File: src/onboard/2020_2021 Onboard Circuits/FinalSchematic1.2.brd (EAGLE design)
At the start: 137.6 x 80 mm, 99 parts, among them IC1 A5975D, IC2 A5975D, IC3 A5975D

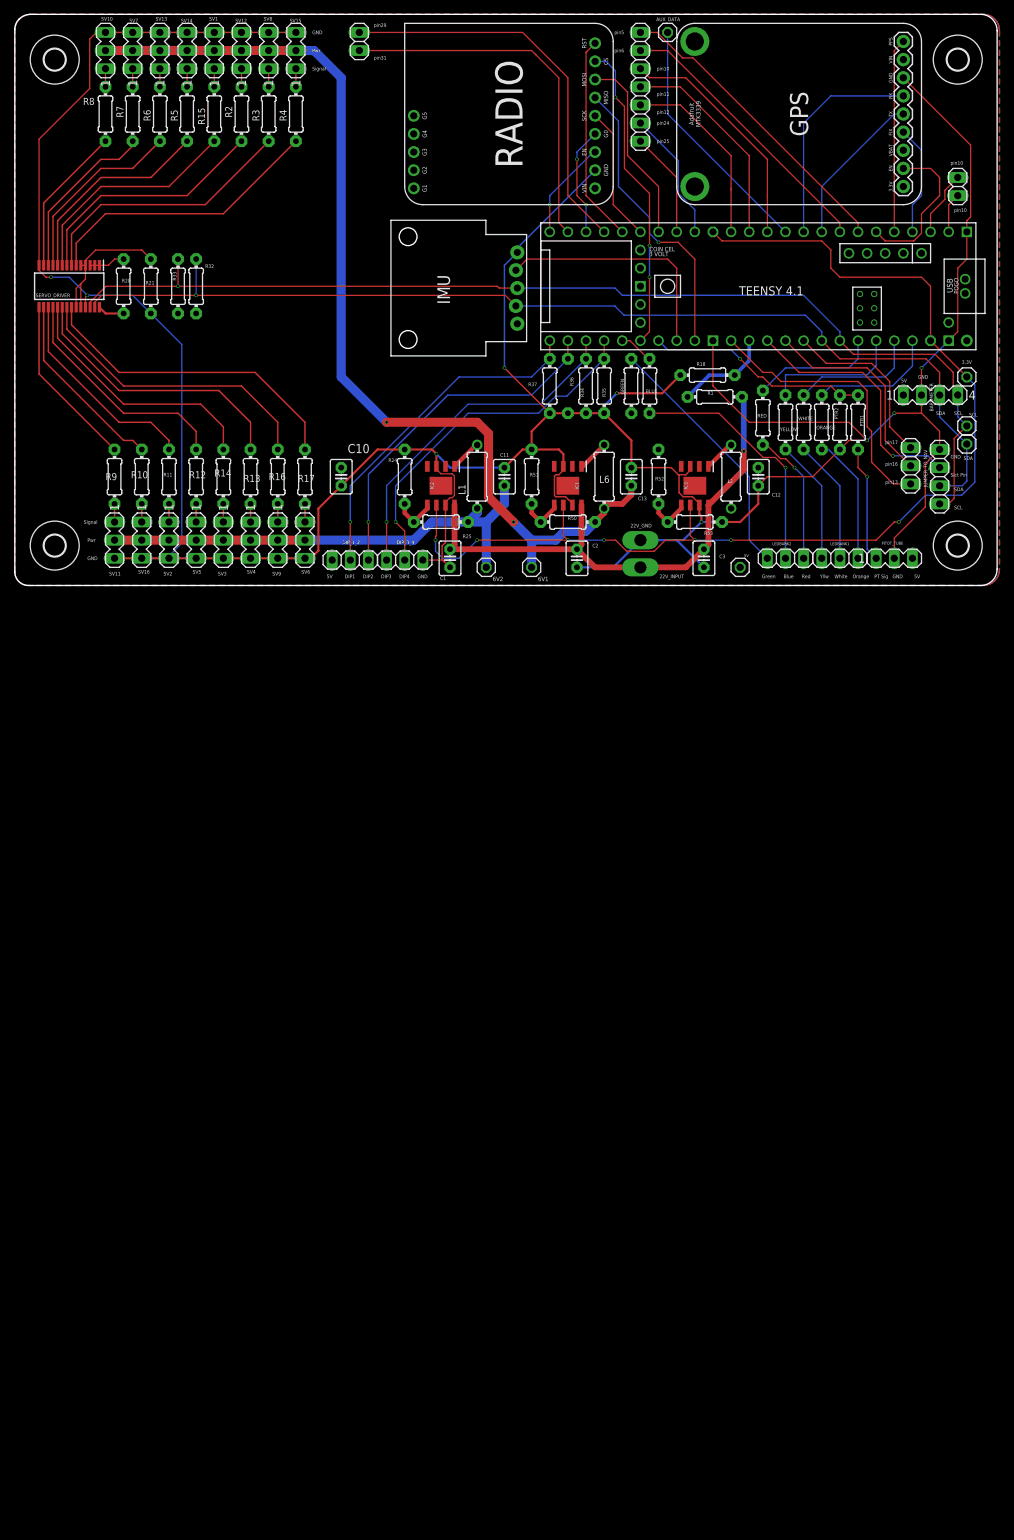
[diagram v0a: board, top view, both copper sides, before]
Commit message: Added button connection, rewired radio, removed pitot tube, split into pages
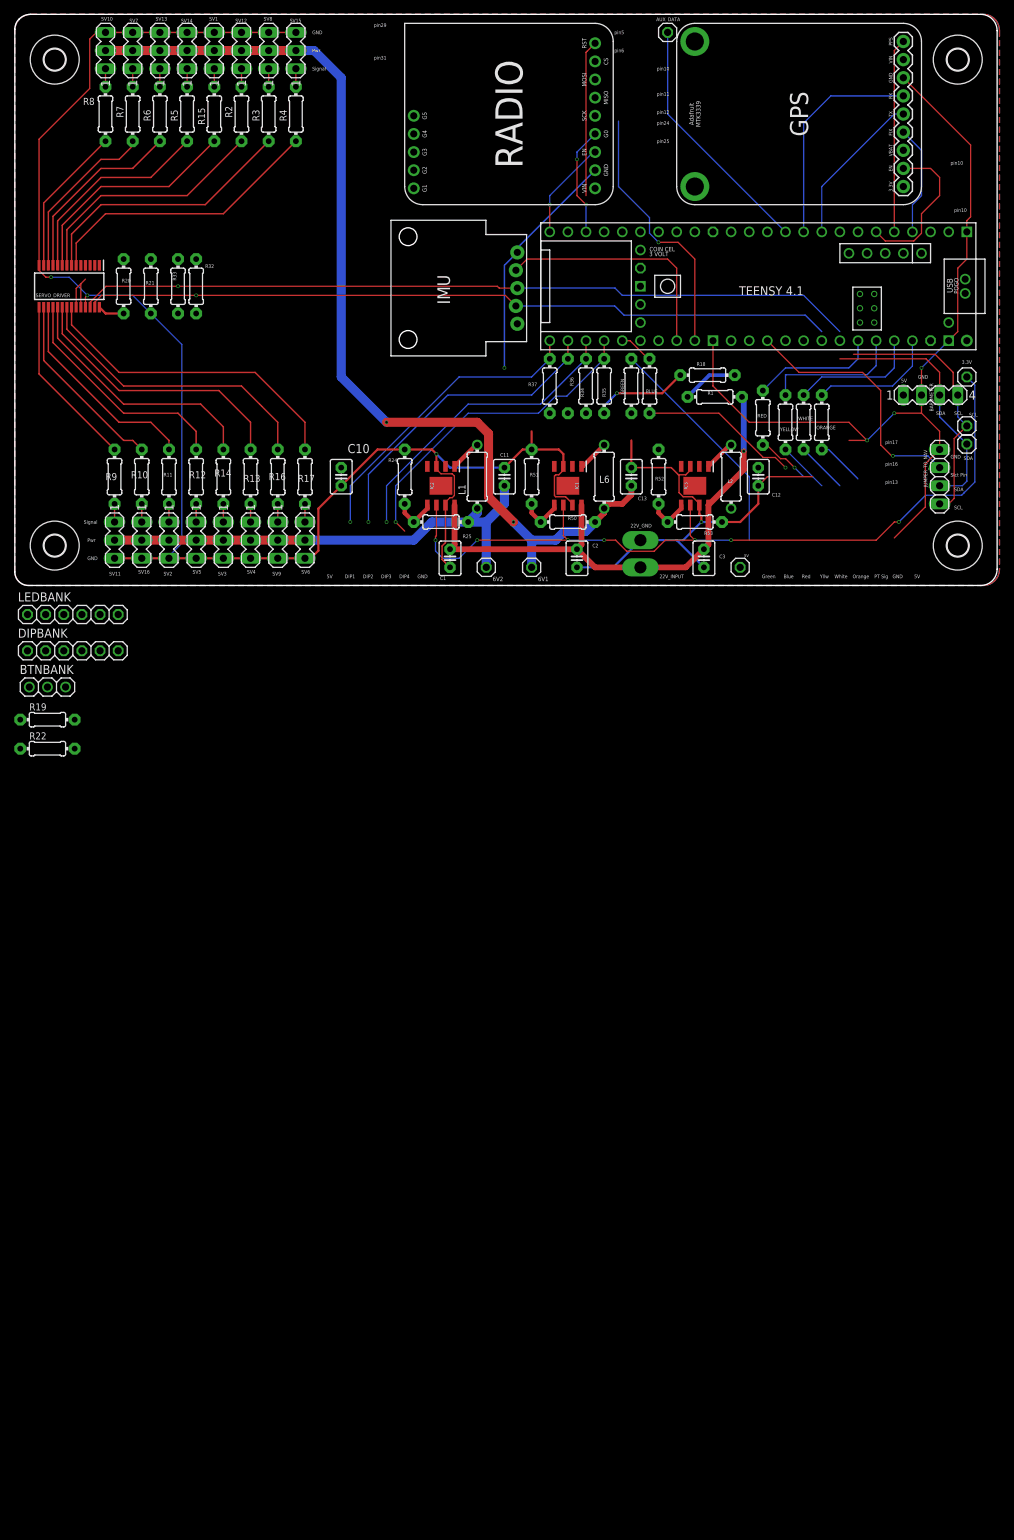
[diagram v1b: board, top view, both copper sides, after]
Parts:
- removed 1, 2, 5: (no value), pinhead:1X02
- removed 4: (no value), pinhead:1X05
- removed DIP_1_2, DIP_3_4, JP1, LEDBANK1, LEDBANK2: (no value), pinhead:1X03
- removed PITOT_TUBE: (no value), con-lstb:MA03-1
- removed PTR1: 2.2K, adafruit:0204/7
- removed PTR2: 4.3K, adafruit:0204/7
- added BTNBANK: (no value), adafruit:1X03
- added DIPBANK, LEDBANK: (no value), adafruit:1X06
- added R19, R22: 2.2k, adafruit:0204/7
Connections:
- removed net MOSI1: RADIO.7, TEENSY4.1.26-A12/MOSI1
- removed net N$4: PITOT_TUBE.1, PTR1.2
- removed net PIN0: 2.2, TEENSY4.1.0-RX1/CS1/CRX2
- removed net PIN1: 2.1, TEENSY4.1.1-TX1/MISO1/CTX2
- removed net PIN10: 4.5, TEENSY4.1.10-CS\MQSR
- removed net PIN11: 4.4, TEENSY4.1.11-MOSI/CTX1
- removed net PIN12: 4.3, TEENSY4.1.12-MISO/MQSL
- removed net PIN13: JP1.3, TEENSY4.1.13-SCK/LED
- removed net PIN14: R1.1, R18.2, TEENSY4.1.14-A0/TX3/SPDIF_OUT
- removed net PIN16: JP1.2, TEENSY4.1.16-A2/RX4/SCL1
- removed net PIN17: JP1.1, TEENSY4.1.17-A3/TX4/SDA1
- removed net PIN24: 4.2, TEENSY4.1.24-A10/TX6/SCL2
- removed net PIN25: 4.1, TEENSY4.1.25-A11/RX6/SDA2
- removed net PIN29: 1.2, TEENSY4.1.29-TX7
- removed net PIN31: 1.1, TEENSY4.1.31-CTX3
- removed net PIN5: 5.2, TEENSY4.1.5-IN2
- removed net PIN6: 5.1, TEENSY4.1.6-OUT1D
- removed net PT_ANLGPIN: PTR1.1, PTR2.2, TEENSY4.1.39-A15/CS/OUT1A
- removed net RADIO_CS: RADIO.8, TEENSY4.1.38-A14/CS/IN1
- removed net SCK1: RADIO.5, TEENSY4.1.27-A13/SCK1
- new net BATLEVEL: R1.1, R18.2
- new net CS0: RADIO.8, TEENSY4.1.10-CS\MQSR
- new net MISO0: RADIO.6, TEENSY4.1.12-MISO/MQSL
- new net MOSI0: RADIO.7, TEENSY4.1.11-MOSI/CTX1
- new net N$3: BTNBANK.1, R22.2
- new net N$5: BTNBANK.2, R19.2
- new net SCK0: RADIO.5, TEENSY4.1.13-SCK/LED
- net 3.3V: now also TEENSY4.1.3V3-2
- net 5V: now also BTNBANK.3, DIPBANK.6, R33.2; no longer DIP_1_2.3, PITOT_TUBE.3, R33.1
- net BLUE: now also LEDBANK.5; no longer LEDBANK2.2
- net DIP1: now also DIPBANK.5; no longer DIP_1_2.2
- net DIP2: now also DIPBANK.4; no longer DIP_1_2.1
- net DIP3: now also DIPBANK.3; no longer DIP_3_4.3
- net DIP4: now also DIPBANK.2; no longer DIP_3_4.2
- net GND: now also DIPBANK.1, R19.1, R22.1, TEENSY4.1.GND2, TEENSY4.1.GND4, TEENSY4.1.GND5; no longer DIP_3_4.1, PITOT_TUBE.2, PTR2.1
- net GNDADDRESS: no longer R21.2
- net GREEN: now also LEDBANK.6; no longer LEDBANK2.3
- net MISO1: no longer RADIO.6
- net ORANGE: now also LEDBANK.1; no longer LEDBANK1.1
- net RADIO_RST: now also TEENSY4.1.6-OUT1D; no longer TEENSY4.1.28-RX7
- net RED: now also LEDBANK.4; no longer LEDBANK2.1
- net SCL: now also R32.1; no longer R33.2
- net SDA: now also R33.1; no longer R32.1
- net WHITE: now also LEDBANK.2; no longer LEDBANK1.2
- net YELLOW: now also LEDBANK.3; no longer LEDBANK1.3
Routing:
- net PIN29: track 55.5 -> 0.00 mm
- net PIN31: track 51.6 -> 0.00 mm
- net 3.3V: track 163.6 -> 113.7 mm
- net RADIO_CS: track 43.7 -> 0.00 mm, vias 3 -> 0
- net PIN5: track 42.8 -> 0.00 mm
- net GND: track 499.0 -> 459.6 mm
- net PIN6: track 39.2 -> 0.00 mm
- net PIN13: track 39.0 -> 0.00 mm
- net PIN10: track 33.2 -> 0.00 mm
- net PT_ANLGPIN: track 31.1 -> 0.00 mm, vias 1 -> 0
- net PIN11: track 29.9 -> 0.00 mm
- net PIN16: track 29.2 -> 0.00 mm
- net MOSI1: track 26.7 -> 0.00 mm
- net PIN12: track 26.3 -> 0.00 mm
- net PIN17: track 24.9 -> 0.00 mm
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
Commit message: Added 5v connector
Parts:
- removed DIPBANK: (no value), adafruit:1X06
- added 5V_PWR: (no value), pinhead:1X03
- added DIPBANK1: (no value), pinhead:1X05
- BTNBANK: device adafruit:1X03 -> pinhead:1X03
- LEDBANK: device adafruit:1X06 -> pinhead:1X06
- moved LEDBANK 29.5 mm to (-27.4, -33.5)
- moved BTNBANK 24.9 mm to (-31.0, -39.1)
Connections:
- net 5V: now also 5V_PWR.1, 5V_PWR.2, DIPBANK1.5; no longer DIPBANK.6
- net DIP1: now also DIPBANK1.4; no longer DIPBANK.5
- net DIP2: now also DIPBANK1.3; no longer DIPBANK.4
- net DIP3: now also DIPBANK1.2; no longer DIPBANK.3
- net DIP4: now also DIPBANK1.1; no longer DIPBANK.2
- net GND: now also 5V_PWR.3; no longer DIPBANK.1

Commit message: Added button wires and fixed 5v input
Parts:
- LEDBANK: device pinhead:1X06 -> pinhead:1X07
- moved LEDBANK 22.4 mm to (-25.9, -55.9)
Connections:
- removed net N$3: BTNBANK.1, R22.2
- removed net N$5: BTNBANK.2, R19.2
- new net BTN1: BTNBANK.2, R19.2, TEENSY4.1.24-A10/TX6/SCL2
- new net BTN2: BTNBANK.1, R22.2, TEENSY4.1.25-A11/RX6/SDA2
- net 5V: now also SV1.2, SV10.2, SV11.2, SV12.2, SV13.2, SV14.2, SV15.2, SV16.2, SV2.2, SV3.2, SV4.2, SV5.2, SV6.2, SV7.2, SV8.2, SV9.2
- net BATLEVEL: now also TEENSY4.1.26-A12/MOSI1
- net BLUE: now also LEDBANK.6; no longer LEDBANK.5
- net GND: now also LEDBANK.1
- net GNDADDRESS: now also R21.2
- net GREEN: now also LEDBANK.7; no longer LEDBANK.6
- net ORANGE: now also LEDBANK.2; no longer LEDBANK.1
- net OUTPUT_BUCK1: no longer SV1.2, SV10.2, SV12.2, SV13.2, SV14.2, SV15.2, SV7.2, SV8.2
- net OUTPUT_BUCK2: no longer SV11.2, SV16.2, SV2.2, SV3.2, SV4.2, SV5.2, SV6.2, SV9.2
- net RED: now also LEDBANK.5; no longer LEDBANK.4
- net WHITE: now also LEDBANK.3; no longer LEDBANK.2
- net YELLOW: now also LEDBANK.4; no longer LEDBANK.3
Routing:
- net 5V: track 3.76 -> 83.8 mm
- net OUTPUT_BUCK2: track 94.7 -> 26.1 mm
- net OUTPUT_BUCK1: track 139.9 -> 110.7 mm

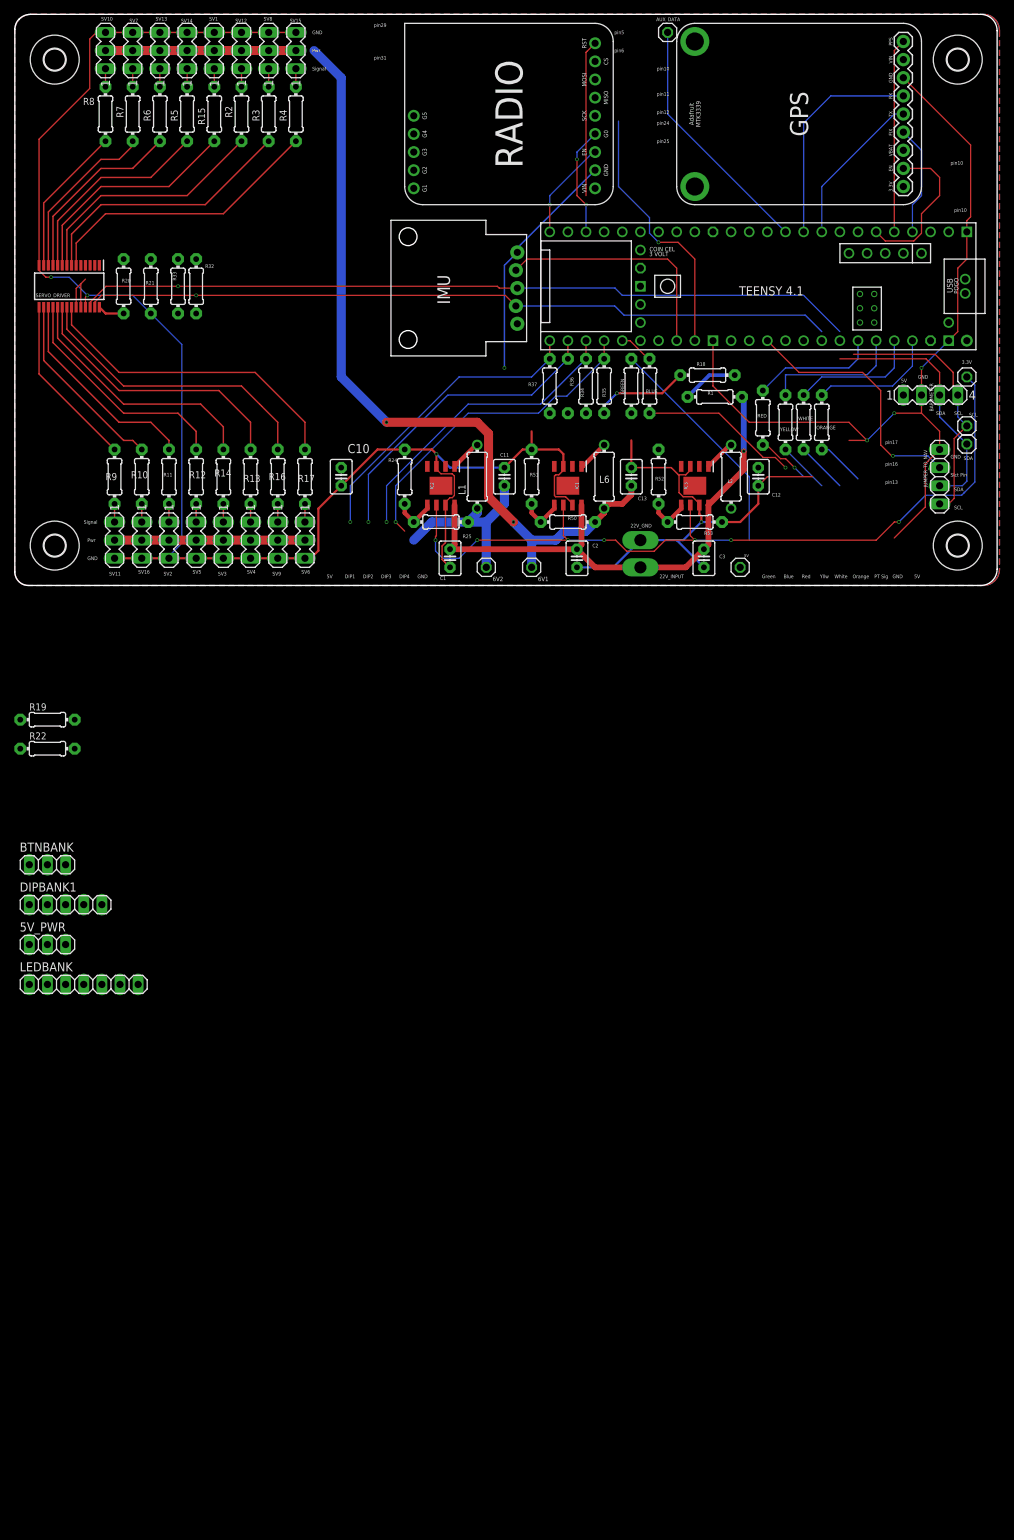
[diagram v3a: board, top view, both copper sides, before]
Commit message: Added 6v->5v LDO regulator
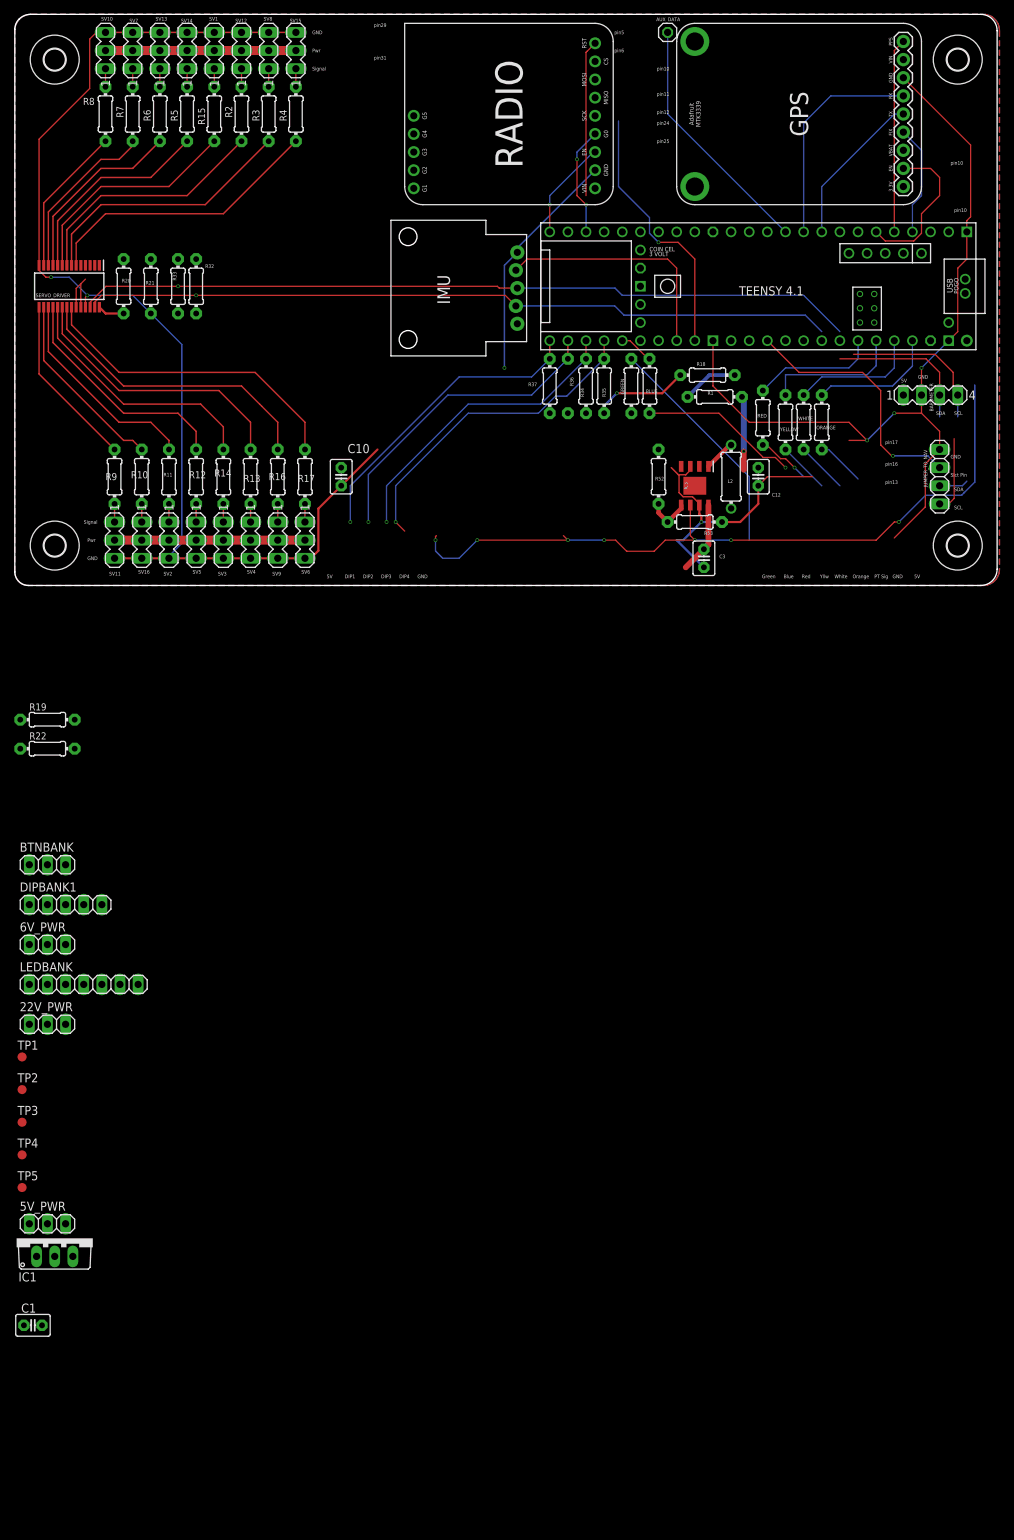
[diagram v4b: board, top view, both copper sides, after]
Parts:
- removed 22V_GND, 22V_INPUT: TPPAD1-17Y, testpad:P1-17Y
- removed 3.3V, 5V, 6V1, 6V2, SCL, SDA: (no value), pinhead:1X01
- removed C11, C13: 470uF, capacitor-wima:C2.5-3
- removed C2: 10uF, capacitor-wima:C2.5-3
- removed IC2: A5975D, A5975D:SOIC127P600X170-9N
- removed L1, L6: 27uH, rcl:TFI0307
- removed R24, R51: 1.5k, adafruit:0204/7
- removed R25, R50: 5.6k, adafruit:0204/7
- added 22V_PWR, 6V_PWR: (no value), pinhead:1X03
- added TP1, TP2, TP3, TP4, TP5: PTR1B1,27, testpad:B1,27
- IC1: value A5975D -> MIC2937A-5.0BT; device A5975D:SOIC127P600X170-9N -> linear:TO220V
- moved IC1 127.6 mm to (-30.0, -91.4), turned to 0 degrees
- moved C1 122.3 mm to (-33.0, -103.6), turned to 0 degrees
- moved 5V_PWR 39.1 mm to (-31.0, -89.4)
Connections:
- removed net N$12: IC2.1, L1.2
- removed net N$19: IC2.5, R24.2, R25.1
- removed net N$8: IC1.1, L6.2
- removed net N$9: IC1.5, R50.1, R51.2
- removed net OUTPUT_BUCK1: 6V1.1, C13.1, L6.1, R50.2
- removed net OUTPUT_BUCK2: 6V2.1, C11.1, L1.1, R25.2
- new net 22V_INPUT: 22V_PWR.1, 22V_PWR.2, C3.1, IC3.8, TP4.TP
- new net 6V: 6V_PWR.1, 6V_PWR.2, IC1.1
- new net N$5: TP5.TP
- net 22_INPUT: no longer 22V_INPUT.TP, C1.1, C2.1, C3.1, IC1.8, IC2.8, IC3.8
- net 3.3V: no longer 3.3V.1, IC1.6, IC2.6
- net 5V: now also C1.1, IC1.3, TP1.TP; no longer 5V.1
- net GND: now also 22V_PWR.3, 6V_PWR.3, IC1.2; no longer 22V_GND.TP, C1.2, C11.2, C13.2, C2.2, IC1.3, IC1.7, IC2.3, IC2.7, R24.1, R51.1
- net SCL: now also TP3.TP; no longer SCL.1
- net SDA: now also TP2.TP; no longer SDA.1
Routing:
- net OUTPUT_BUCK1: track 110.7 -> 0.00 mm, vias 2 -> 0
- net GND: track 459.6 -> 373.3 mm, vias 9 -> 8
- net 22_INPUT: track 74.3 -> 10.3 mm
- net OUTPUT_BUCK2: track 26.1 -> 0.00 mm
- net SDA: track 140.7 -> 130.1 mm
- net 3.3V: track 113.7 -> 103.6 mm
- net 22V_INPUT: track 0.00 -> 10.0 mm
- net N$9: track 6.22 -> 0.00 mm
- net N$19: track 6.22 -> 0.00 mm
- net N$8: track 4.42 -> 0.00 mm
- net N$12: track 4.42 -> 0.00 mm
- net SCL: track 145.8 -> 141.5 mm
